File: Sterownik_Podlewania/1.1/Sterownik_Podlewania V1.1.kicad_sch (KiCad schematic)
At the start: 30 parts, among them J12 Conn_01x04_Socket, J7 RJ45, J8 RJ45, J9 RJ45, U10 ESP32-DEVKITC, U7 757, U9 757

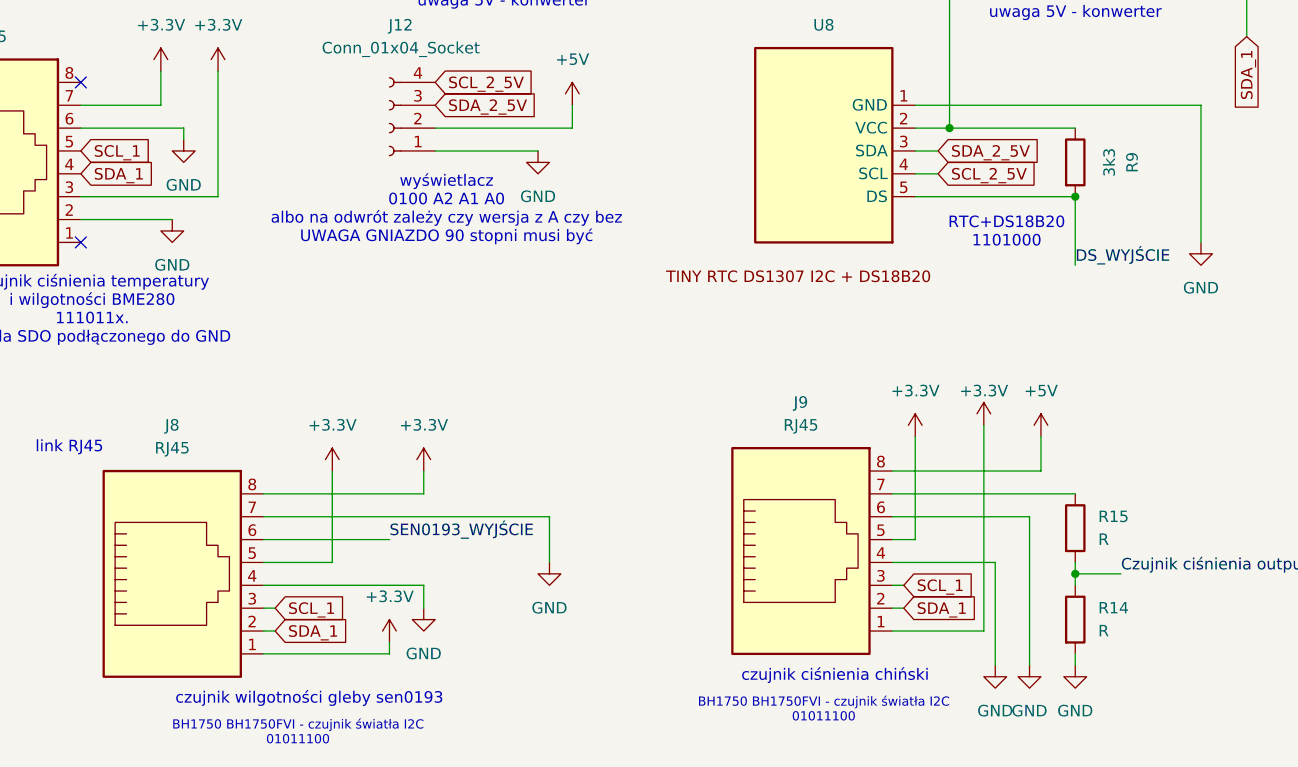
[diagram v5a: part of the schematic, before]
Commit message: Kod websocket, kod stonka demo, kod sterownika - wszystkie taski poza bt wstepnie ogarniete
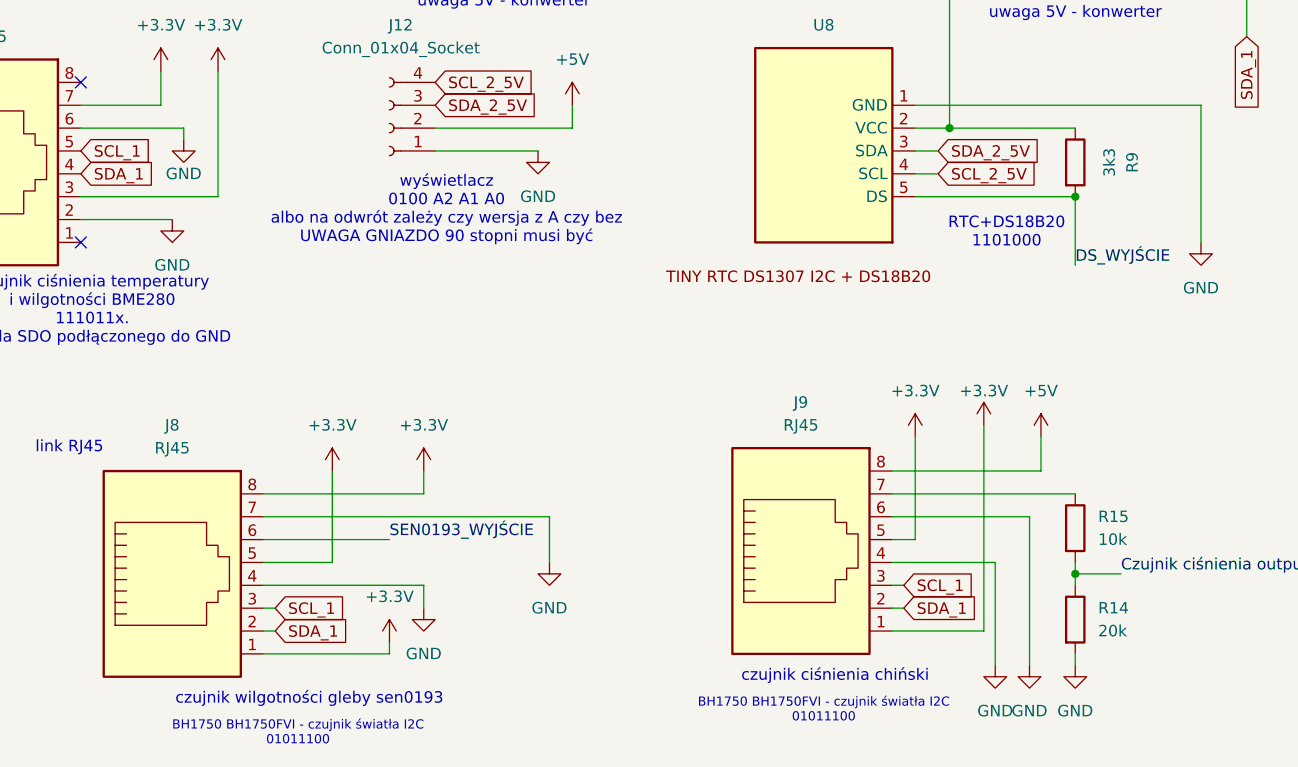
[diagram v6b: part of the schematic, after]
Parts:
- R14: value R -> 20k
- R15: value R -> 10k
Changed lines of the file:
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@@
 			)
 		)
-		(property "Value" "R"
+		(property "Value" "10k"
 			(at 147.32 171.4499 0)
 			(effects
@@
 			)
 		)
-		(property "Value" "R"
+		(property "Value" "20k"
 			(at 147.32 181.6099 0)
 			(effects
@@
 		(on_board yes)
 		(dnp no)
-		(fields_autoplaced yes)
 		(property "Reference" "#PWR04"
 			(at 45.72 133.35 0)
@@
 		)
 		(property "Value" "GND"
-			(at 45.72 132.08 0)
-			(effects
-				(font
+			(at 45.72 130.81 0)
+			(effects
+				(font
